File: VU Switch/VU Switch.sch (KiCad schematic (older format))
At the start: 4 parts, among them M1 Mounting_pin, M2 Mounting_pin, M3 Mounting_pin, M4 Mounting_pin

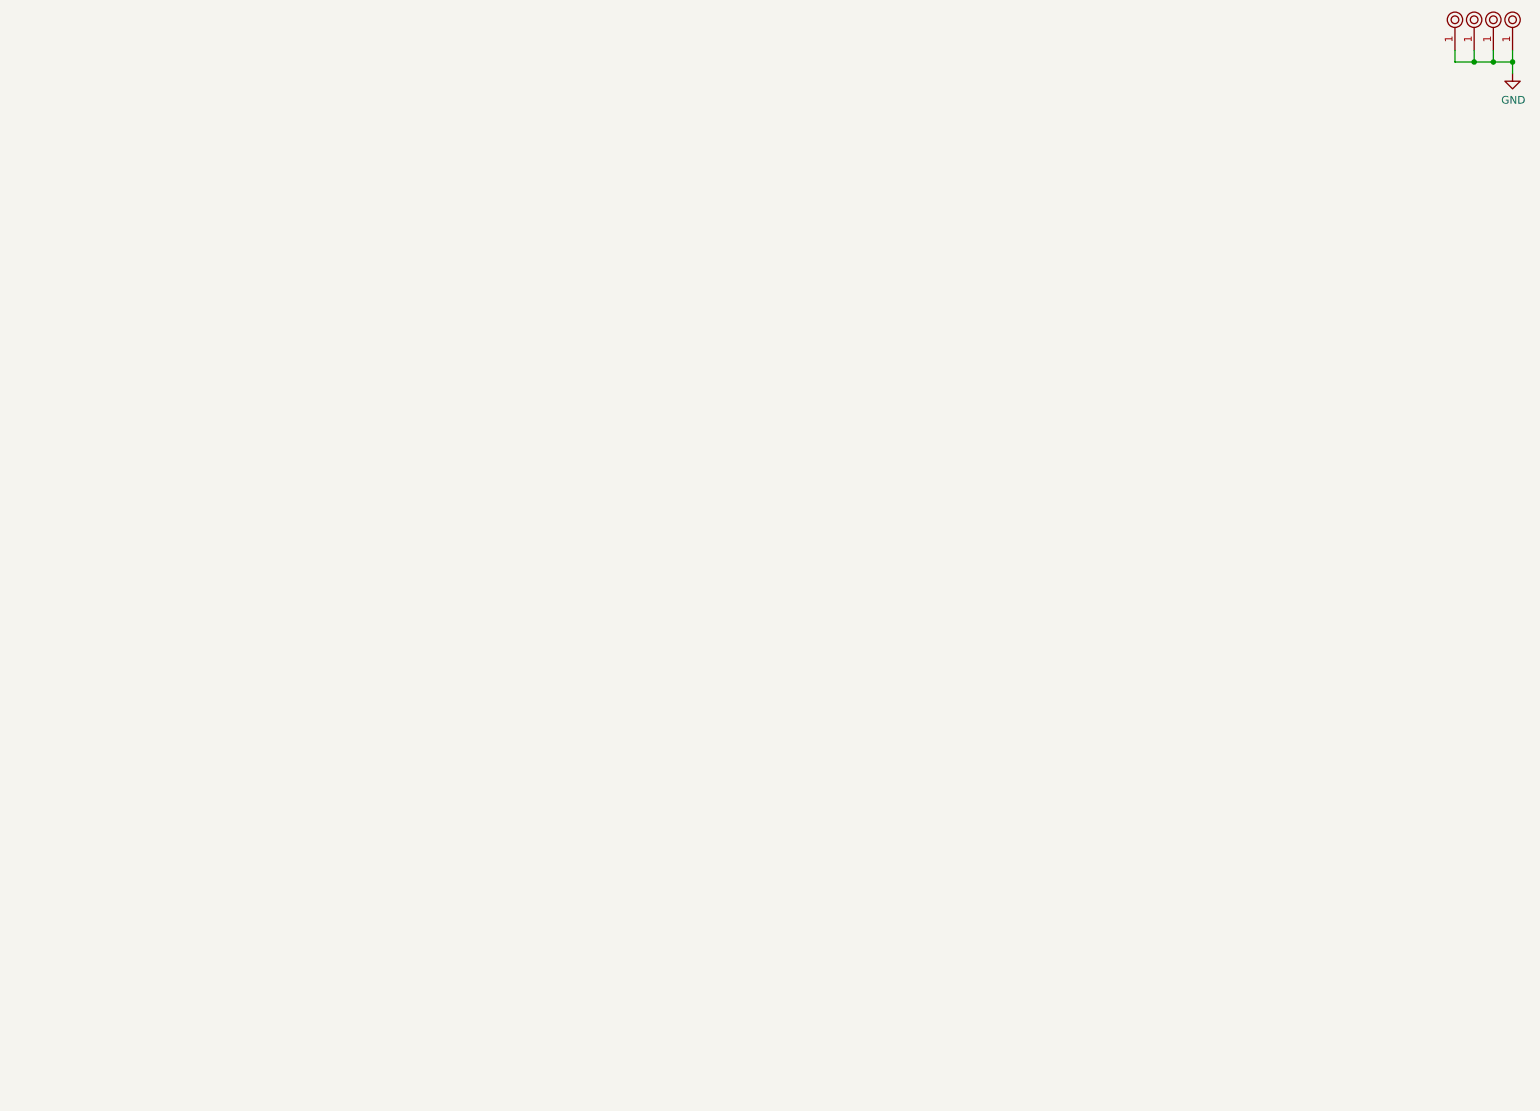
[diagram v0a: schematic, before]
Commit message: Schematic done
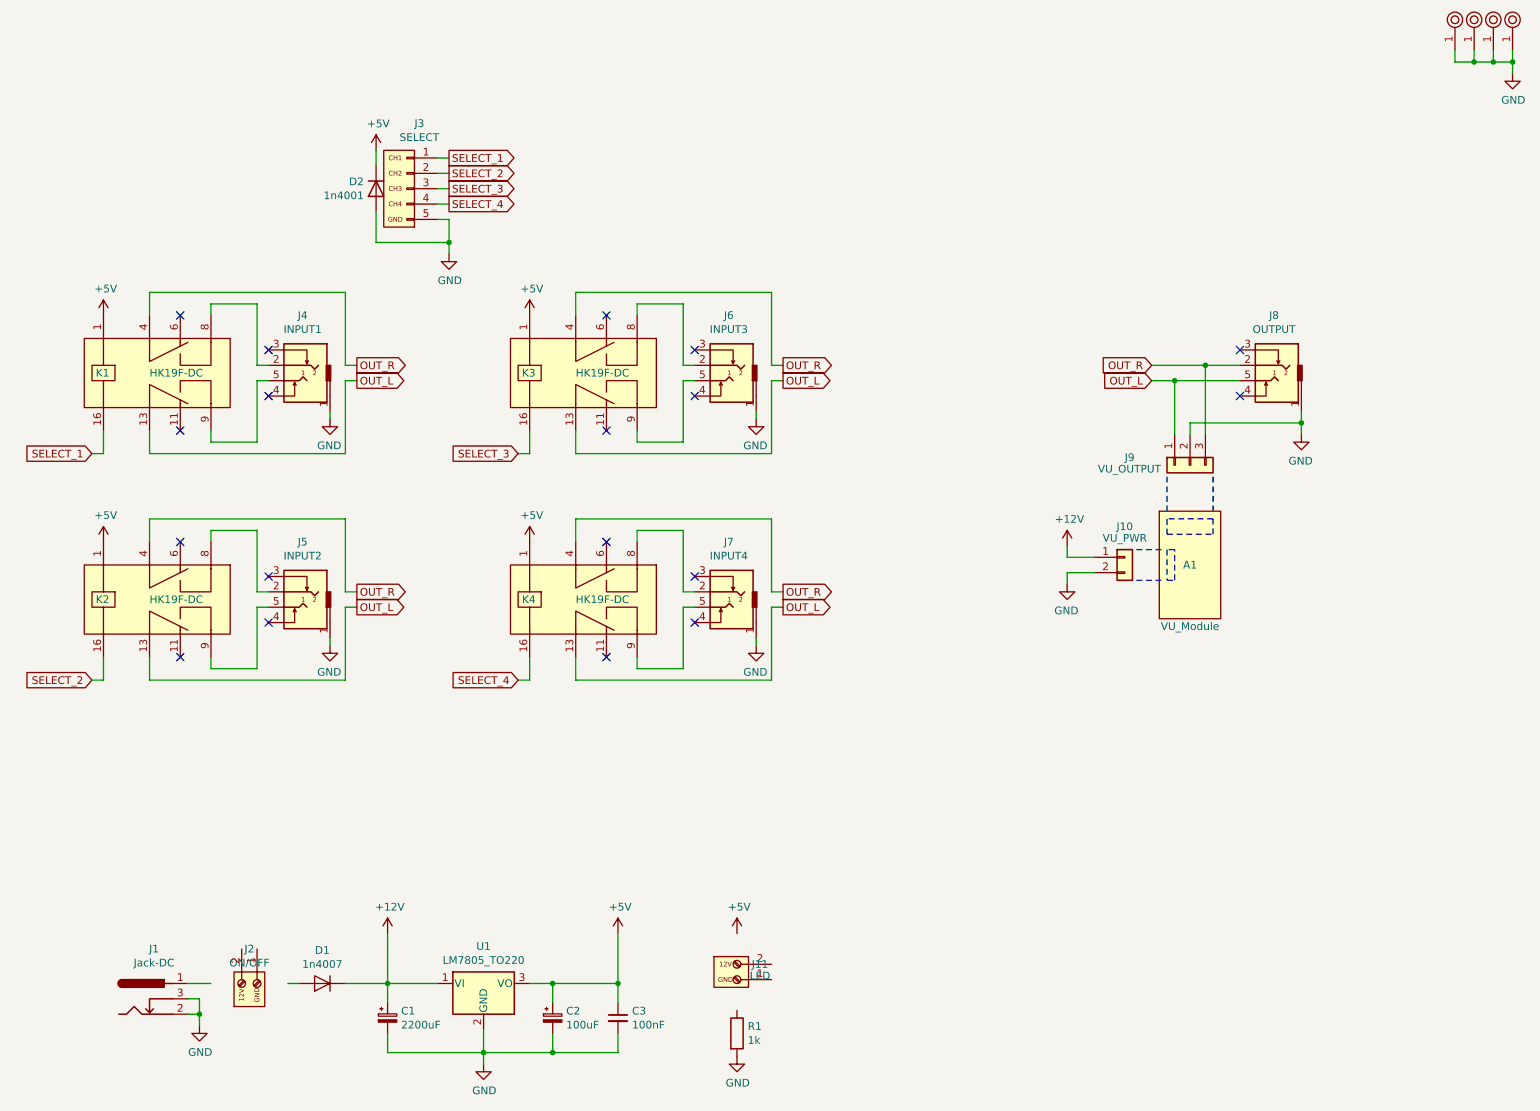
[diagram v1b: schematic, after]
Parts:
- added A1: VU_Module, VU Switch:VU_Driver_Board_5.0, symbol VU_Switch:VU_Module
- added C1: 2200uF, symbol Device:CP_Small
- added C2: 100uF, symbol Device:CP_Small
- added C3: 100nF, symbol Device:C_Small
- added D1: 1n4007, symbol barrel_jack:reverse_protect
- added D2: 1n4001, symbol Device:D
- added J1: Jack-DC, symbol barrel_jack:barrel_12v
- added J10: VU_PWR, symbol Connector_Generic:Conn_01x02
- added J11: LED, symbol VU_Switch:PWR
- added J2: ON/OFF, symbol VU_Switch:PWR
- added J3: SELECT, symbol VU_Switch:SELECT
- added J4: INPUT1, symbol audio_jack:TRS_3.5mm
- added J5: INPUT2, symbol audio_jack:TRS_3.5mm
- added J6: INPUT3, symbol audio_jack:TRS_3.5mm
- added J7: INPUT4, symbol audio_jack:TRS_3.5mm
- added J8: OUTPUT, symbol audio_jack:TRS_3.5mm
- added J9: VU_OUTPUT, symbol Connector_Generic:Conn_01x03
- added K1, K2, K3, K4: HK19F-DC, symbol hk19f-dc:HK19F-DC
- added R1: 1k, symbol Device:R
- added U1: LM7805_TO220, Package_TO_SOT_THT:TO-220-3_Vertical, symbol Regulator_Linear:LM7805_TO220
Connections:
- net GND: now also C1.2, C2.2, C3.2, D2.2 (A), J1.2, J1.3, J10.2 (Pin_2), J3.5 (Pin_5), J4.1, J5.1, J6.1, J7.1, J8.1, J9.2 (Pin_2), R1.2, U1.2 (GND)
- new net: J4.2, K1.8 (NO_1)
- new net: J4.5, K1.9 (NO_2)
- new net: J5.2, K2.8 (NO_1)
- new net: J5.5, K2.9 (NO_2)
- new net: J6.2, K3.8 (NO_1)
- new net: J6.5, K3.9 (NO_2)
- new net: J7.2, K4.8 (NO_1)
- new net: J7.5, K4.9 (NO_2)
- new net +12V: C1.1, D1.1 (K), J10.1 (Pin_1), U1.1 (VI)
- new net +5V: C2.1, C3.1, D2.1 (K), K1.1, K2.1, K3.1, K4.1, U1.3 (VO)
- new net OUT_L: J8.5, J9.1 (Pin_1), K1.13 (COM_2), K2.13 (COM_2), K3.13 (COM_2), K4.13 (COM_2)
- new net OUT_R: J8.2, J9.3 (Pin_3), K1.4 (COM_1), K2.4 (COM_1), K3.4 (COM_1), K4.4 (COM_1)
- new net SELECT_1: J3.1 (Pin_1), K1.16
- new net SELECT_2: J3.2 (Pin_2), K2.16
- new net SELECT_3: J3.3 (Pin_3), K3.16
- new net SELECT_4: J3.4 (Pin_4), K4.16
- no-connect marks 0 -> 18

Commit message: Assigned footprints
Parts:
- added J12: VU_5V, Connector_JST:JST_XH_B2B-XH-A_1x02_P2.50mm_Vertical, symbol VU_Switch:VU_5V
- C1: footprint (none) -> Capacitor_THT:CP_Radial_D13.0mm_P5.00mm
- C2, C3: footprint (none) -> Capacitor_THT:CP_Radial_D6.3mm_P2.50mm
- D1, D2: footprint (none) -> Diodes_THT:D_DO-41_SOD81_P10.16mm_Horizontal
- J1: footprint (none) -> Connector_BarrelJack:BarrelJack_Horizontal
- J10: value VU_PWR -> VU_12V; footprint (none) -> Connector_JST:JST_XH_B2B-XH-A_1x02_P2.50mm_Vertical; symbol Connector_Generic:Conn_01x02 -> VU_Switch:VU_12V
- J11: footprint (none) -> Connector_JST:JST_XH_B2B-XH-A_1x02_P2.50mm_Vertical
- J2: footprint (none) -> Connector_PinHeader_2.54mm:PinHeader_1x02_P2.54mm_Vertical
- J3: footprint (none) -> Connector_JST:JST_XH_B5B-XH-A_1x05_P2.50mm_Vertical
- J4, J5, J6, J7, J8: footprint (none) -> audio_jack:Tayda_3.5mm_stereo_TRS_jack_A-853
- J9: value VU_OUTPUT -> VU_OUT; footprint (none) -> Connector_JST:JST_XH_B2B-XH-A_1x02_P2.50mm_Vertical; symbol Connector_Generic:Conn_01x03 -> VU_Switch:VU_OUT
- K1, K2, K3, K4: footprint (none) -> HK19F-DC:HK19F-DC
- R1: footprint (none) -> Resistor_THT:R_Axial_DIN0207_L6.3mm_D2.5mm_P10.16mm_Horizontal
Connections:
- net +12V: now also J10.2 (Pin_2); no longer J10.1 (Pin_1)
- net +5V: now also J12.2 (Pin_2)
- net GND: now also J10.1 (Pin_1), J12.1 (Pin_1); no longer J10.2 (Pin_2)
- net OUT_L: now also J9.3 (Pin_3); no longer J9.1 (Pin_1)
- net OUT_R: now also J9.1 (Pin_1); no longer J9.3 (Pin_3)
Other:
- moved on the sheet: D2, J3, J8

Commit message: Layout done
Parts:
- removed J1: Jack-DC, Connector_BarrelJack:BarrelJack_Horizontal, symbol barrel_jack:barrel_12v
- added J13, J2: VU_12V, Connector_JST:JST_XH_B2B-XH-A_1x02_P2.50mm_Vertical, symbol VU_Switch:VU_12V
- C3: footprint Capacitor_THT:CP_Radial_D6.3mm_P2.50mm -> Capacitor_THT:C_Disc_D4.7mm_W2.5mm_P5.00mm
- D1, D2: footprint Diodes_THT:D_DO-41_SOD81_P10.16mm_Horizontal -> Diode_THT:D_DO-41_SOD81_P10.16mm_Horizontal
- J1: renamed from J2; value ON/OFF -> DC_12V; footprint Connector_PinHeader_2.54mm:PinHeader_1x02_P2.54mm_Vertical -> TerminalBlock:TerminalBlock_bornier-2_P5.08mm
- J11: symbol VU_Switch:PWR -> VU_Switch:LED
- J9: footprint Connector_JST:JST_XH_B2B-XH-A_1x02_P2.50mm_Vertical -> Connector_JST:JST_XH_B3B-XH-A_1x03_P2.50mm_Vertical
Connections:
- net +12V: now also J13.2 (Pin_2), J2.2 (Pin_2)
- net +5V: now also J11.2 (Pin_2)
- net GND: now also J1.1 (Pin_1), J13.1 (Pin_1), J2.1 (Pin_1)
- net at D1.2 (A): now also J1.2 (Pin_2)
- net at R1.1: now also J11.1 (Pin_1)
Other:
- moved on the sheet: J1
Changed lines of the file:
@@
 $EndComp
-$Comp
-L barrel_jack:barrel_12v J1
-U 1 1 600505BB
-P 2050 6950
-F 0 "J1" H 2129 7275 50  0000 C CNN
-F 1 "Jack-DC" H 2129 7184 50  0000 C CNN
-F 2 "Connector_BarrelJack:BarrelJack_Horizontal" H 2100 6910 50  0001 C CNN
-F 3 "~" H 2100 6910 50  0001 C CNN
-	1    2050 6950
-	1    0    0    -1
-$EndComp
-Wire Wire Line
-	2350 6950 2425 6950
-Wire Wire Line
-	2425 6950 2425 7050
-Wire Wire Line
-	2425 7050 2350 7050
-Wire Wire Line
-	2425 7050 2425 7125
-Connection ~ 2425 7050
 $Comp
 L power:GND #PWR0102
 U 1 1 600515E6
-P 2425 7125
-F 0 "#PWR0102" H 2425 6875 50  0001 C CNN
-F 1 "GND" H 2430 6952 50  0000 C CNN
-F 2 "" H 2425 7125 50  0001 C CNN
-F 3 "" H 2425 7125 50  0001 C CNN
-	1    2425 7125
+P 3000 7025
+F 0 "#PWR0102" H 3000 6775 50  0001 C CNN
+F 1 "GND" H 3005 6852 50  0000 C CNN
+F 2 "" H 3000 7025 50  0001 C CNN
+F 3 "" H 3000 7025 50  0001 C CNN
+	1    3000 7025
 	1    0    0    -1
 $EndComp
@@
 F 0 "D1" H 3225 6634 50  0000 C CNN
 F 1 "1n4007" H 3225 6725 50  0000 C CNN
-F 2 "Diodes_THT:D_DO-41_SOD81_P10.16mm_Horizontal" H 3225 6850 50  0001 C CNN
+F 2 "Diode_THT:D_DO-41_SOD81_P10.16mm_Horizontal" H 3225 6850 50  0001 C CNN
 F 3 "~" H 3225 6850 50  0001 C CNN
 	1    3225 6850
 	-1   0    0    1
 $EndComp
-Wire Wire Line
-	2350 6850 2500 6850
 $Comp
 L power:+12V #PWR0103
@@
 F 0 "D2" V 3504 1480 50  0000 L CNN
 F 1 "1n4001" V 3595 1480 50  0000 L CNN
-F 2 "Diodes_THT:D_DO-41_SOD81_P10.16mm_Horizontal" H 3550 1400 50  0001 C CNN
+F 2 "Diode_THT:D_DO-41_SOD81_P10.16mm_Horizontal" H 3550 1400 50  0001 C CNN
 F 3 "~" H 3550 1400 50  0001 C CNN
 	1    3550 1400
@@
 F 0 "C3" H 5242 7121 50  0000 L CNN
 F 1 "100nF" H 5242 7030 50  0000 L CNN
-F 2 "Capacitor_THT:CP_Radial_D6.3mm_P2.50mm" H 5150 7075 50  0001 C CNN
+F 2 "Capacitor_THT:C_Disc_D4.7mm_W2.5mm_P5.00mm" H 5150 7075 50  0001 C CNN
 F 3 "~" H 5150 7075 50  0001 C CNN
 	1    5150 7075
@@
 $EndComp
 $Comp
-L VU_Switch:PWR J2
+L VU_Switch:PWR J1
 U 1 1 600737D5
 P 2700 6850
-F 0 "J2" V 2925 6800 50  0000 C CNN
-F 1 "ON/OFF" V 2834 6800 50  0000 C CNN
-F 2 "Connector_PinHeader_2.54mm:PinHeader_1x02_P2.54mm_Vertical" H 2700 6850 50  0001 C CNN
+F 0 "J1" H 2675 7050 50  0000 C CNN
+F 1 "DC_12V" H 2675 6975 50  0000 C CNN
+F 2 "TerminalBlock:TerminalBlock_bornier-2_P5.08mm" H 2700 6850 50  0001 C CNN
 F 3 "~" H 2700 6850 50  0001 C CNN
 	1    2700 6850
-	0    -1   -1   0
-$EndComp
-Wire Wire Line
-	3075 6850 3000 6850
+	1    0    0    -1
+$EndComp
 $Comp
 L audio_jack:TRS_3.5mm J8
@@
 F 0 "J9" V 8850 3750 50  0000 R CNN
 F 1 "VU_OUT" V 8925 3950 50  0000 R CNN
-F 2 "Connector_JST:JST_XH_B2B-XH-A_1x02_P2.50mm_Vertical" H 8875 3475 50  0001 C CNN
+F 2 "Connector_JST:JST_XH_B3B-XH-A_1x03_P2.50mm_Vertical" H 8875 3475 50  0001 C CNN
 F 3 "~" H 8875 3475 50  0001 C CNN
 	1    8875 3475
@@
 L power:+12V #PWR011
 U 1 1 60179B78
-P 8025 4000
-F 0 "#PWR011" H 8025 3850 50  0001 C CNN
-F 1 "+12V" H 8040 4173 50  0000 C CNN
-F 2 "" H 8025 4000 50  0001 C CNN
-F 3 "" H 8025 4000 50  0001 C CNN
-	1    8025 4000
-	1    0    0    -1
-$EndComp
-Wire Wire Line
-	8025 4000 8025 4075
-Wire Wire Line
-	8025 4175 8025 4250
+P 8025 3825
+F 0 "#PWR011" H 8025 3675 50  0001 C CNN
+F 1 "+12V" H 8040 3998 50  0000 C CNN
+F 2 "" H 8025 3825 50  0001 C CNN
+F 3 "" H 8025 3825 50  0001 C CNN
+	1    8025 3825
+	1    0    0    -1
+$EndComp
+Wire Wire Line
+	7950 4325 7950 4400
 $Comp
 L power:GND #PWR012
 U 1 1 601869EE
-P 8025 4250
-F 0 "#PWR012" H 8025 4000 50  0001 C CNN
-F 1 "GND" H 8030 4077 50  0000 C CNN
-F 2 "" H 8025 4250 50  0001 C CNN
-F 3 "" H 8025 4250 50  0001 C CNN
-	1    8025 4250
+P 7950 4400
+F 0 "#PWR012" H 7950 4150 50  0001 C CNN
+F 1 "GND" H 7955 4227 50  0000 C CNN
+F 2 "" H 7950 4400 50  0001 C CNN
+F 3 "" H 7950 4400 50  0001 C CNN
+	1    7950 4400
 	-1   0    0    -1
 $EndComp
@@
 	9025 3925 9025 3825
 Wire Wire Line
-	8025 4175 8200 4175
-Wire Wire Line
 	8025 4075 8200 4075
 Wire Wire Line
@@
 $EndComp
 $Comp
-L VU_Switch:PWR J11
+L VU_Switch:LED J11
 U 1 1 602A90B3
 P 5925 6725
@@
 	8975 2825 9325 2825
 Connection ~ 8975 2825
+Wire Wire Line
+	2925 6850 3075 6850
+Wire Wire Line
+	2925 6950 3000 6950
+Wire Wire Line
+	3000 6950 3000 7025
+$Comp
+L VU_Switch:VU_12V J2
+U 1 1 601FAC2C
+P 7675 3975
+F 0 "J2" H 7875 3975 50  0000 C CNN
+F 1 "VU_12V" H 7975 3875 50  0000 C CNN
+F 2 "Connector_JST:JST_XH_B2B-XH-A_1x02_P2.50mm_Vertical" H 7675 3975 50  0001 C CNN
+F 3 "~" H 7675 3975 50  0001 C CNN
+	1    7675 3975
+	-1   0    0    -1
+$EndComp
+$Comp
+L VU_Switch:VU_12V J13
+U 1 1 60208FDA
+P 7675 4225
+F 0 "J13" H 7875 4225 50  0000 C CNN
+F 1 "VU_12V" H 7975 4125 50  0000 C CNN
+F 2 "Connector_JST:JST_XH_B2B-XH-A_1x02_P2.50mm_Vertical" H 7675 4225 50  0001 C CNN
+F 3 "~" H 7675 4225 50  0001 C CNN
+	1    7675 4225
+	-1   0    0    -1
+$EndComp
+Wire Wire Line
+	8025 3825 8025 3975
+Wire Wire Line
+	8025 4075 8025 4225
+Connection ~ 8025 4075
+Connection ~ 8025 3975
+Wire Wire Line
+	8025 3975 8025 4075
+Wire Wire Line
+	7950 4075 7950 4175
+Wire Wire Line
+	7875 3975 8025 3975
+Wire Wire Line
+	7875 4225 8025 4225
+Wire Wire Line
+	7875 4075 7950 4075
+Wire Wire Line
+	7875 4325 7950 4325
+Wire Wire Line
+	8200 4175 7950 4175
+Connection ~ 7950 4175
+Wire Wire Line
+	7950 4175 7950 4325
+Connection ~ 7950 4325
 $EndSCHEMATC

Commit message: Changed HK19 relay footprint to larger pads
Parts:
- J11: symbol VU_Switch:LED -> VU_Switch:LED_Plugin
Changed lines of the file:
@@
 $EndComp
 $Comp
-L VU_Switch:LED J11
+L VU_Switch:LED_Plugin J11
 U 1 1 602A90B3
-P 5925 6725
-F 0 "J11" H 6075 6725 50  0000 C CNN
-F 1 "LED" H 6075 6650 50  0000 C CNN
-F 2 "Connector_JST:JST_XH_B2B-XH-A_1x02_P2.50mm_Vertical" H 5925 6725 50  0001 C CNN
-F 3 "~" H 5925 6725 50  0001 C CNN
-	1    5925 6725
-	1    0    0    -1
+P 5925 6700
+F 0 "J11" H 5800 6800 50  0000 C CNN
+F 1 "LED" H 6025 6800 50  0000 C CNN
+F 2 "Connector_JST:JST_XH_B2B-XH-A_1x02_P2.50mm_Vertical" H 5925 6700 50  0001 C CNN
+F 3 "~" H 5925 6700 50  0001 C CNN
+	1    5925 6700
+	0    -1   -1   0
 $EndComp
 $Comp
 L power:+5V #PWR0108
 U 1 1 602B3872
-P 5925 6525
-F 0 "#PWR0108" H 5925 6375 50  0001 C CNN
-F 1 "+5V" H 5940 6698 50  0000 C CNN
-F 2 "" H 5925 6525 50  0001 C CNN
-F 3 "" H 5925 6525 50  0001 C CNN
-	1    5925 6525
+P 5925 6400
+F 0 "#PWR0108" H 5925 6250 50  0001 C CNN
+F 1 "+5V" H 5940 6573 50  0000 C CNN
+F 2 "" H 5925 6400 50  0001 C CNN
+F 3 "" H 5925 6400 50  0001 C CNN
+	1    5925 6400
 	1    0    0    -1
 $EndComp
